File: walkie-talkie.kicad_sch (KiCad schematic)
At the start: 12 parts, among them J1 I2C, J2 Conn_01x08, J3 esp32-pico-kit, J4 speakers, SW1 Transmit, SW2 POWER, U1 tp4056, U2 adafruit-MAX98357, U3 mems-mic

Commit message: Add mounting holes
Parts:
- added H1, H2, H3: MountingHole, MountingHole:MountingHole_3.2mm_M3, symbol Mechanical:MountingHole
- U1: value tp4056 -> WARNING: Switch off when Plugging in Power on the ESP
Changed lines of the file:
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@@
+    )
+  )
+  (symbol (lib_id "Mechanical:MountingHole") (at 38.1 132.08 0) (unit 1)
+    (in_bom yes) (on_board yes) (dnp no) (fields_autoplaced)
+    (property "Reference" "H2" (at 40.64 130.81 0)
+      (effects (font (size 1.27 1.27)) (justify left))
+    )
+    (property "Value" "MountingHole" (at 40.64 133.35 0)
+      (effects (font (size 1.27 1.27)) (justify left))
+    )
+    (property "Footprint" "MountingHole:MountingHole_3.2mm_M3" (at 38.1 132.08 0)
+      (effects (font (size 1.27 1.27)) hide)
+    )
+    (property "Datasheet" "~" (at 38.1 132.08 0)
+      (effects (font (size 1.27 1.27)) hide)
+    )
+    (instances
+      (project "walkie-talkie"
+        (path "/61e03e29-1a6a-43b3-bf57-7ccd770a7463"
+          (reference "H2") (unit 1)
+        )
+      )
     )
   )
@@
         (path "/61e03e29-1a6a-43b3-bf57-7ccd770a7463"
           (reference "#PWR017") (unit 1)
+        )
+      )
+    )
+  )
+  (symbol (lib_id "Mechanical:MountingHole") (at 38.1 124.46 0) (unit 1)
+    (in_bom yes) (on_board yes) (dnp no) (fields_autoplaced)
+    (property "Reference" "H1" (at 40.64 123.19 0)
+      (effects (font (size 1.27 1.27)) (justify left))
+    )
+    (property "Value" "MountingHole" (at 40.64 125.73 0)
+      (effects (font (size 1.27 1.27)) (justify left))
+    )
+    (property "Footprint" "MountingHole:MountingHole_3.2mm_M3" (at 38.1 124.46 0)
+      (effects (font (size 1.27 1.27)) hide)
+    )
+    (property "Datasheet" "~" (at 38.1 124.46 0)
+      (effects (font (size 1.27 1.27)) hide)
+    )
+    (instances
+      (project "walkie-talkie"
+        (path "/61e03e29-1a6a-43b3-bf57-7ccd770a7463"
+          (reference "H1") (unit 1)
         )
       )
@@
     )
   )
+  (symbol (lib_id "Mechanical:MountingHole") (at 38.1 139.7 0) (unit 1)
+    (in_bom yes) (on_board yes) (dnp no) (fields_autoplaced)
+    (property "Reference" "H3" (at 40.64 138.43 0)
+      (effects (font (size 1.27 1.27)) (justify left))
+    )
+    (property "Value" "MountingHole" (at 40.64 140.97 0)
+      (effects (font (size 1.27 1.27)) (justify left))
+    )
+    (property "Footprint" "MountingHole:MountingHole_3.2mm_M3" (at 38.1 139.7 0)
+      (effects (font (size 1.27 1.27)) hide)
+    )
+    (property "Datasheet" "~" (at 38.1 139.7 0)
+      (effects (font (size 1.27 1.27)) hide)
+    )
+    (instances
+      (project "walkie-talkie"
+        (path "/61e03e29-1a6a-43b3-bf57-7ccd770a7463"
+          (reference "H3") (unit 1)
+        )
+      )
+    )
+  )
   (symbol (lib_id "power:GND") (at 59.69 58.42 0) (unit 1)
     (in_bom yes) (on_board yes) (dnp no) (fields_autoplaced)
@@
   )
   (symbol (lib_id "tp4056:tp4056") (at 59.69 49.53 0) (unit 1)
-    (in_bom yes) (on_board yes) (dnp no) (fields_autoplaced)
+    (in_bom yes) (on_board yes) (dnp no)
     (property "Reference" "U1" (at 61.8841 38.1 0)
       (effects (font (size 1.27 1.27)) (justify left))
     )
-    (property "Value" "tp4056" (at 61.8841 40.64 0)
-      (effects (font (size 1.27 1.27)) (justify left))
-    )
+    (property "Value" "WARNING: Switch off when Plugging in Power on the ESP" (at 68.58 36.83 0)
+      (effects (font (size 1.27 1.27)) (justify left))
+    )

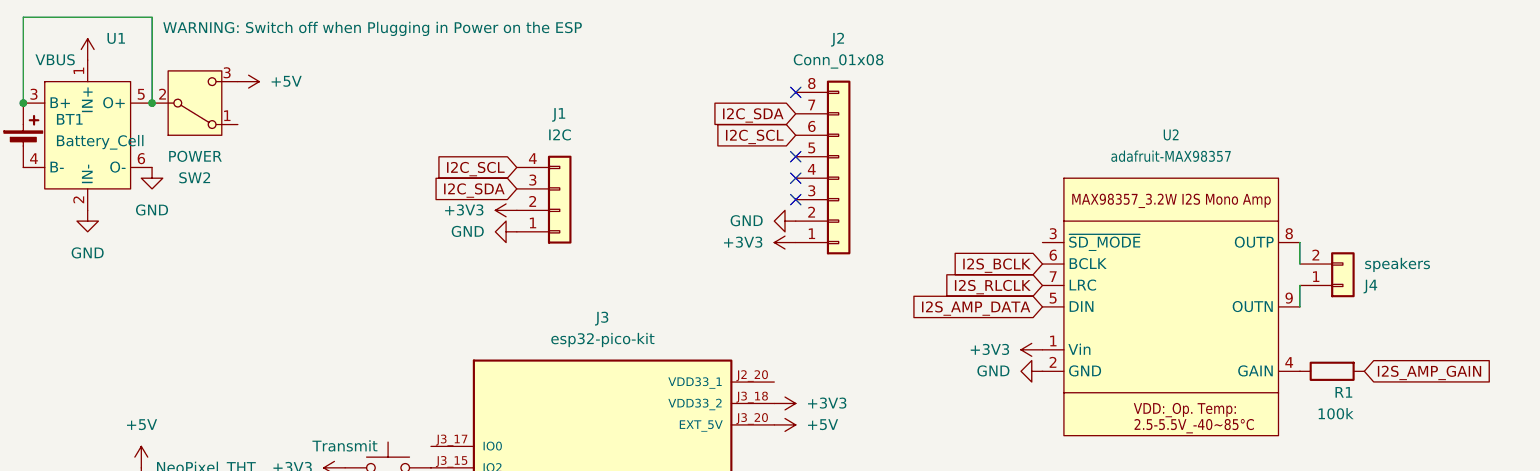
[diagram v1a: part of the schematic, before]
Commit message: Add CVS speaker
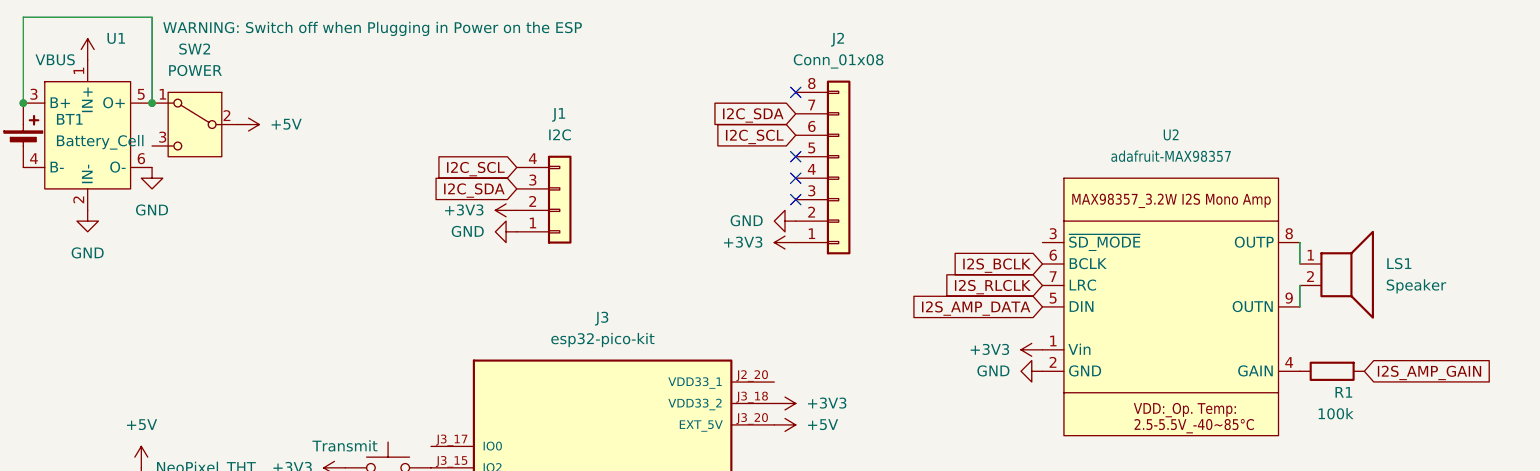
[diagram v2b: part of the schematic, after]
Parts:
- removed J4: speakers, Connector_JST:JST_XA_B02B-XASK-1_1x02_P2.50mm_Vertical, symbol Connector_Generic:Conn_01x02
- added LS1: Speaker, Connector_PinSocket_2.54mm:PinSocket_1x04_P2.54mm_Horizontal, symbol Device:Speaker
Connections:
- net +5V: now also SW2.2 (B); no longer SW2.3 (C)
- net at U2.8 (OUTP): now also LS1.1
- net at U2.9 (OUTN): now also LS1.2
- net at BT1.1 (+), U1.3 (B+), U1.5 (O+): now also SW2.1 (A); no longer SW2.2 (B)
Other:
- moved on the sheet: SW2
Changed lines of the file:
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@@
 (kicad_sch (version 20230121) (generator eeschema)
   (paper "A4")
+  (junction (at 67.31 45.72) (diameter 0) (color 0 0 0 0)
+  )
   (junction (at 52.07 45.72) (diameter 0) (color 0 0 0 0)
   )
   (junction (at 140.97 149.86) (diameter 0) (color 0 0 0 0)
-  )
-  (junction (at 67.31 45.72) (diameter 0) (color 0 0 0 0)
   )
   (no_connect (at 143.51 54.61))
@@
     (stroke (width 0) (type default))
   )
-  (wire (pts (xy 67.31 35.56) (xy 67.31 45.72))
-    (stroke (width 0) (type default))
-  )
   (wire (pts (xy 203.2 67.31) (xy 203.2 69.85))
     (stroke (width 0) (type default))
@@
   )
   (wire (pts (xy 203.2 62.23) (xy 203.2 64.77))
+    (stroke (width 0) (type default))
+  )
+  (wire (pts (xy 67.31 35.56) (xy 67.31 45.72))
     (stroke (width 0) (type default))
   )
@@
     )
   )
-  (symbol (lib_id "Connector_Generic:Conn_01x02") (at 208.28 67.31 0) (mirror x) (unit 1)
-    (in_bom yes) (on_board yes) (dnp no)
-    (property "Reference" "J4" (at 210.82 67.31 0)
-      (effects (font (size 1.27 1.27)) (justify left))
-    )
-    (property "Value" "speakers" (at 210.82 64.77 0)
-      (effects (font (size 1.27 1.27)) (justify left))
-    )
-    (property "Footprint" "Connector_JST:JST_XA_B02B-XASK-1_1x02_P2.50mm_Vertical" (at 208.28 67.31 0)
-      (effects (font (size 1.27 1.27)) hide)
-    )
-    (property "Datasheet" "~" (at 208.28 67.31 0)
-      (effects (font (size 1.27 1.27)) hide)
-    )
-    (pin "1")
-    (pin "2")
-    (instances
-      (project "walkie-talkie"
-        (path "/61e03e29-1a6a-43b3-bf57-7ccd770a7463"
-          (reference "J4") (unit 1)
-        )
-      )
-    )
-  )
   (symbol (lib_id "power:+5V") (at 140.97 83.82 270) (unit 1)
     (in_bom yes) (on_board yes) (dnp no) (fields_autoplaced)
@@
     )
   )
-  (symbol (lib_id "power:+5V") (at 77.47 43.18 270) (unit 1)
-    (in_bom yes) (on_board yes) (dnp no) (fields_autoplaced)
-    (property "Reference" "#PWR04" (at 73.66 43.18 0)
-      (effects (font (size 1.27 1.27)) hide)
-    )
-    (property "Value" "+5V" (at 81.28 43.18 90)
-      (effects (font (size 1.27 1.27)) (justify left))
-    )
-    (property "Footprint" "" (at 77.47 43.18 0)
-      (effects (font (size 1.27 1.27)) hide)
-    )
-    (property "Datasheet" "" (at 77.47 43.18 0)
+  (symbol (lib_id "power:+5V") (at 77.47 48.26 270) (unit 1)
+    (in_bom yes) (on_board yes) (dnp no) (fields_autoplaced)
+    (property "Reference" "#PWR04" (at 73.66 48.26 0)
+      (effects (font (size 1.27 1.27)) hide)
+    )
+    (property "Value" "+5V" (at 81.28 48.26 90)
+      (effects (font (size 1.27 1.27)) (justify left))
+    )
+    (property "Footprint" "" (at 77.47 48.26 0)
+      (effects (font (size 1.27 1.27)) hide)
+    )
+    (property "Datasheet" "" (at 77.47 48.26 0)
       (effects (font (size 1.27 1.27)) hide)
     )
@@
         (path "/61e03e29-1a6a-43b3-bf57-7ccd770a7463"
           (reference "U3") (unit 1)
+        )
+      )
+    )
+  )
+  (symbol (lib_id "Device:Speaker") (at 208.28 64.77 0) (unit 1)
+    (in_bom yes) (on_board yes) (dnp no) (fields_autoplaced)
+    (property "Reference" "LS1" (at 213.36 64.77 0)
+      (effects (font (size 1.27 1.27)) (justify left))
+    )
+    (property "Value" "Speaker" (at 213.36 67.31 0)
+      (effects (font (size 1.27 1.27)) (justify left))
+    )
+    (property "Footprint" "Connector_PinSocket_2.54mm:PinSocket_1x04_P2.54mm_Horizontal" (at 208.28 69.85 0)
+      (effects (font (size 1.27 1.27)) hide)
+    )
+    (property "Datasheet" "~" (at 208.026 66.04 0)
+      (effects (font (size 1.27 1.27)) hide)
+    )
+    (pin "1")
+    (pin "2")
+    (instances
+      (project "walkie-talkie"
+        (path "/61e03e29-1a6a-43b3-bf57-7ccd770a7463"
+          (reference "LS1") (unit 1)
         )
       )
@@
     )
   )
-  (symbol (lib_id "Switch:SW_SPDT") (at 72.39 45.72 0) (mirror x) (unit 1)
+  (symbol (lib_id "Switch:SW_SPDT") (at 72.39 48.26 0) (mirror y) (unit 1)
     (in_bom yes) (on_board yes) (dnp no)
-    (property "Reference" "SW2" (at 72.39 54.61 0)
-      (effects (font (size 1.27 1.27)))
-    )
-    (property "Value" "POWER" (at 72.39 52.07 0)
-      (effects (font (size 1.27 1.27)))
-    )
-    (property "Footprint" "Button_Switch_SMD:SW_SPDT_CK-JS102011SAQN" (at 72.39 45.72 0)
-      (effects (font (size 1.27 1.27)) hide)
-    )
-    (property "Datasheet" "~" (at 72.39 38.1 0)
-      (effects (font (size 1.27 1.27)) hide)
-    )
+    (property "Reference" "SW2" (at 72.39 39.37 0)
+      (effects (font (size 1.27 1.27)))
+    )
+    (property "Value" "POWER" (at 72.39 41.91 0)
+      (effects (font (size 1.27 1.27)))
+    )
+    (property "Footprint" "Button_Switch_SMD:SW_SPDT_CK-JS102011SAQN" (at 72.39 48.26 0)
+      (effects (font (size 1.27 1.27)) hide)
+    )
+    (property "Datasheet" "~" (at 72.39 55.88 0)
+      (effects (font (size 1.27 1.27)) hide)
+    )

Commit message: Lolin32-Lite PCB
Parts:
- removed BT1: Battery_Cell, Connector_JST:JST_XA_B02B-XASK-1_1x02_P2.50mm_Vertical, symbol Device:Battery_Cell
- removed J2: Conn_01x08, Connector_PinHeader_2.54mm:PinHeader_1x08_P2.54mm_Vertical, symbol Connector_Generic:Conn_01x08
- removed J3: esp32-pico-kit, esp32-pico-kit:esp32-pico-kit, symbol esp32-pico-kit:esp32-pico-kit
- removed SW1: Transmit, pts636:pts636, symbol Switch:SW_Push
- removed U1: WARNING: Switch off when Plugging in Power on the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, tp4056:tp4056, symbol tp4056:tp4056
- added SW2: Transmit, pts636:pts636, symbol Switch:SW_Push
- added U1: ~, lolin32-lite:lolin32-lite, symbol lolin32-lite:lolin32-lite
- renumbered SW2 to SW1
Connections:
- net +3V3: now also D1.3 (VDD), SW1.1 (A), SW2.2, U1.26 (3V3)
- net GND: now also SW1.3 (C), U1.13 (GND)
- net I2C_SCL: now also U1.10 (IO28)
- net I2C_SDA: now also U1.9 (IO26)
- net I2S_AMP_DATA: now also U1.21 (IO5)
- net I2S_AMP_GAIN: now also U1.20 (IO17)
- net I2S_BCLK: now also U1.22 (IO18)
- net I2S_MIC_DATA: now also U1.14 (IO13)
- net I2S_RLCLK: now also U1.23 (IO23)
- net at D1.4 (DIN): now also U1.24 (IO19)
- net +5V: no longer names the net of SW1.2 (B)
- net +5V: now also U1.3 (EN); no longer D1.3 (VDD)
- new net: SW2.1, U1.25 (IO22)
- no-connect marks 4 -> 0
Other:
- moved on the sheet: D1, H1, H2, H3, SW1
